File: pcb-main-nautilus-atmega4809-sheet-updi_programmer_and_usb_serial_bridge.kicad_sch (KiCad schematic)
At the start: 7 parts, among them U3 ATSAMD11D14A-SS

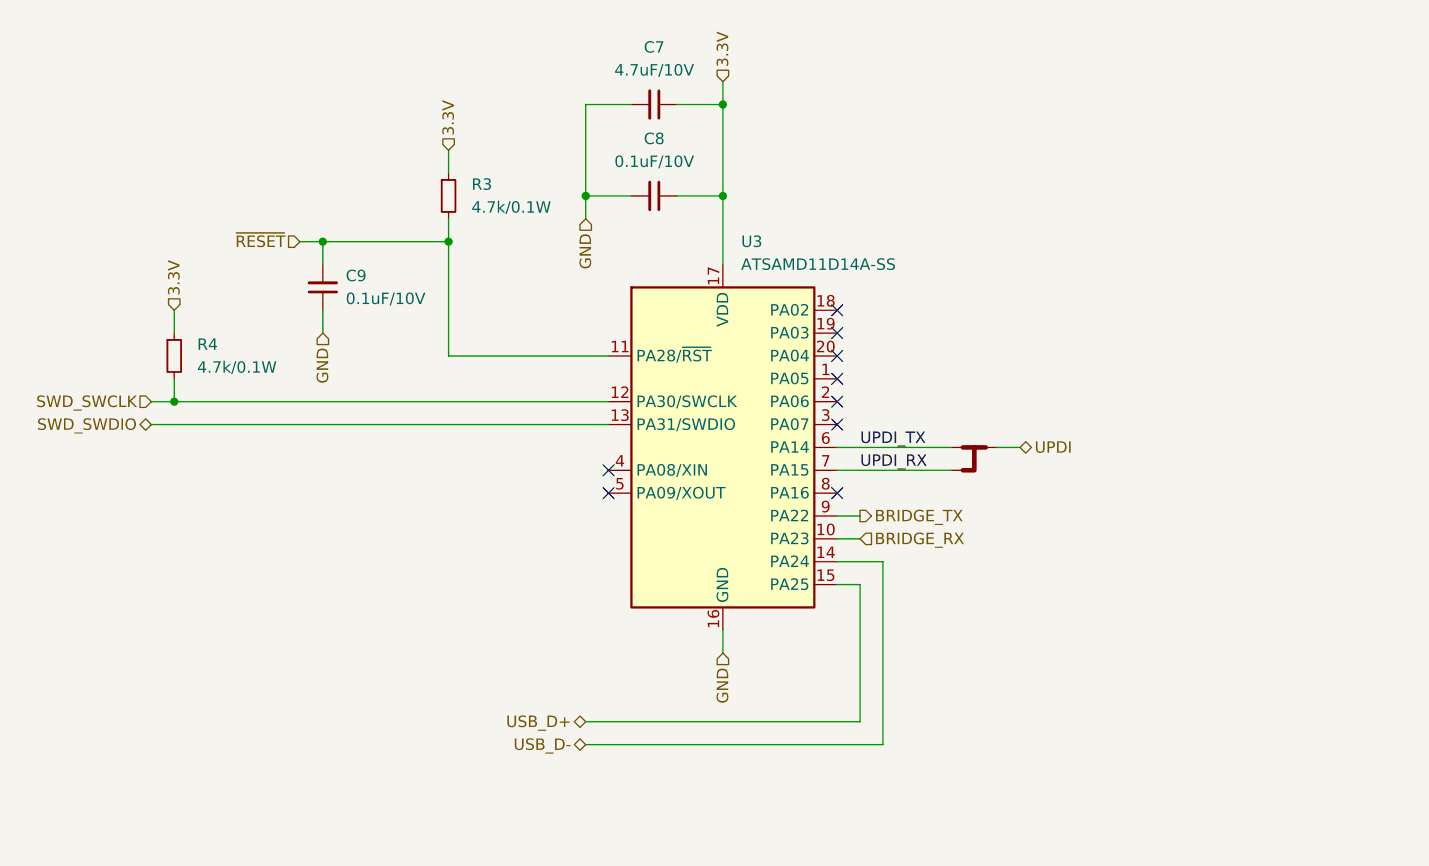
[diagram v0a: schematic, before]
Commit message: Improve UDPI programmer and USB-serial bridge sheet flow
Supports #2.
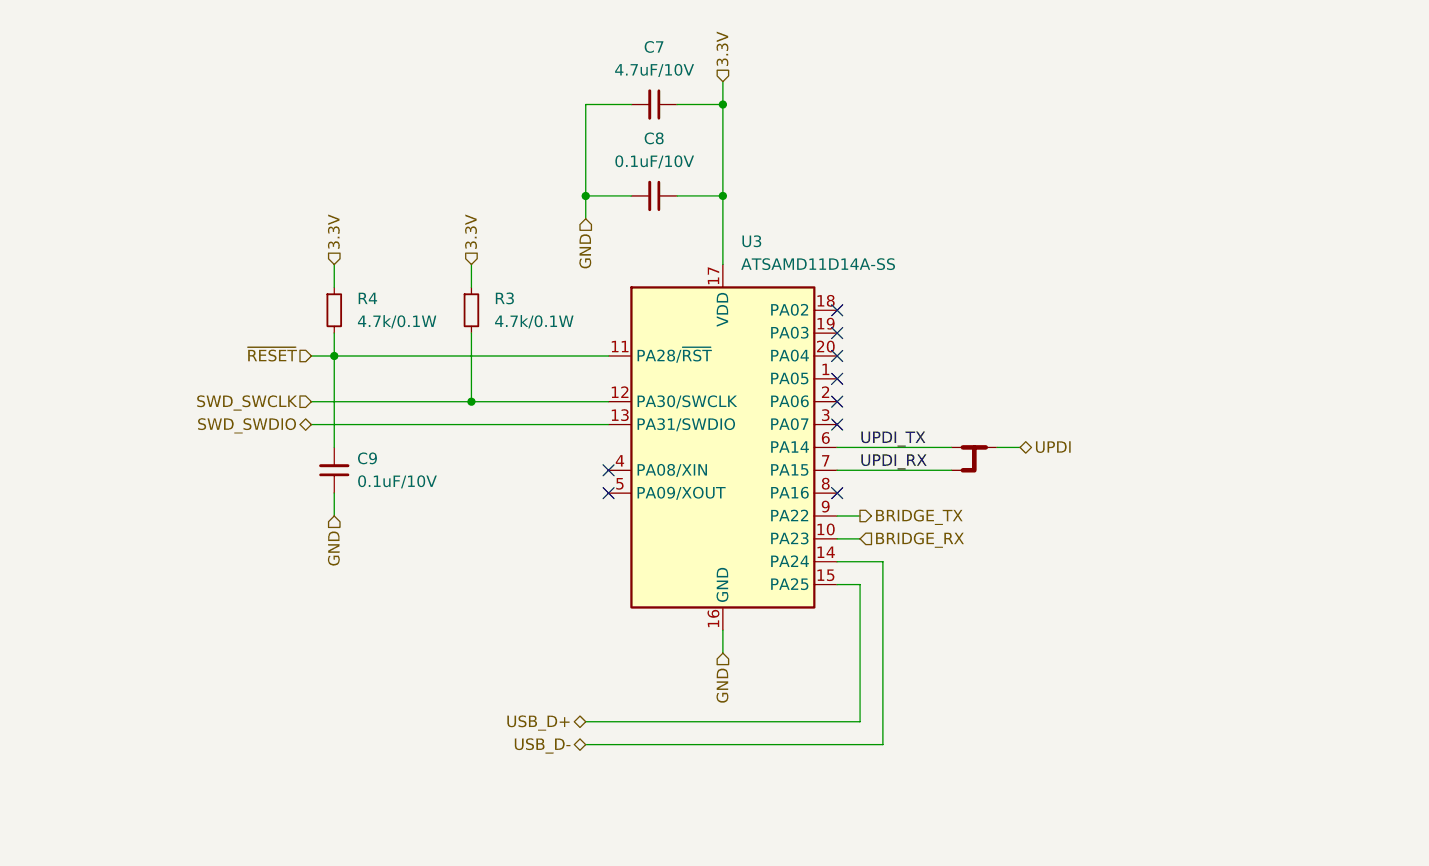
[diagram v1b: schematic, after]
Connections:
- net SWD_SWCLK: now also R3.2; no longer R4.2
- net ~{RESET}: now also R4.2; no longer R3.2
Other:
- moved on the sheet: C9, R3, R4

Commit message: Update schematic annotations
Supports #2.
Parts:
- renumbered R4 to R3, R3 to R4
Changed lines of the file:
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@@
   (symbol (lib_id "Device:R_Small") (at 111.76 86.36 0) (unit 1)
     (in_bom yes) (on_board yes) (fields_autoplaced)
-    (property "Reference" "R3" (id 0) (at 114.3 85.0899 0)
+    (property "Reference" "R4" (id 0) (at 114.3 85.0899 0)
       (effects (font (size 1.27 1.27)) (justify left))
     )
@@
   (symbol (lib_id "Device:R_Small") (at 96.52 86.36 0) (unit 1)
     (in_bom yes) (on_board yes) (fields_autoplaced)
-    (property "Reference" "R4" (id 0) (at 99.06 85.0899 0)
+    (property "Reference" "R3" (id 0) (at 99.06 85.0899 0)
       (effects (font (size 1.27 1.27)) (justify left))
     )

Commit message: Connect root sheet
Supports #2.
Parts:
- renumbered C9 to C10, C7 to C8, C8 to C9, R3 to R4, R4 to R5
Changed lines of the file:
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@@
   (symbol (lib_id "Device:C_Small") (at 96.52 104.14 180) (unit 1)
     (in_bom yes) (on_board yes) (fields_autoplaced)
-    (property "Reference" "C9" (id 0) (at 99.06 102.8635 0)
+    (property "Reference" "C10" (id 0) (at 99.06 102.8635 0)
       (effects (font (size 1.27 1.27)) (justify right))
     )
@@
   (symbol (lib_id "Device:C_Small") (at 132.08 73.66 270) (unit 1)
     (in_bom yes) (on_board yes) (fields_autoplaced)
-    (property "Reference" "C8" (id 0) (at 132.0736 67.31 90))
+    (property "Reference" "C9" (id 0) (at 132.0736 67.31 90))
     (property "Value" "0.1uF/10V" (id 1) (at 132.0736 69.85 90))
     (property "Footprint" "Capacitor_SMD:C_0603_1608Metric_Pad1.08x0.95mm_HandSolder" (id 2) (at 132.08 73.66 0)
@@
   (symbol (lib_id "Device:R_Small") (at 111.76 86.36 0) (unit 1)
     (in_bom yes) (on_board yes) (fields_autoplaced)
-    (property "Reference" "R4" (id 0) (at 114.3 85.0899 0)
+    (property "Reference" "R5" (id 0) (at 114.3 85.0899 0)
       (effects (font (size 1.27 1.27)) (justify left))
     )
@@
   (symbol (lib_id "Device:C_Small") (at 132.08 63.5 270) (unit 1)
     (in_bom yes) (on_board yes) (fields_autoplaced)
-    (property "Reference" "C7" (id 0) (at 132.0736 57.15 90))
+    (property "Reference" "C8" (id 0) (at 132.0736 57.15 90))
     (property "Value" "4.7uF/10V" (id 1) (at 132.0736 59.69 90))
     (property "Footprint" "Capacitor_SMD:C_0603_1608Metric_Pad1.08x0.95mm_HandSolder" (id 2) (at 132.08 63.5 0)
@@
   (symbol (lib_id "Device:R_Small") (at 96.52 86.36 0) (unit 1)
     (in_bom yes) (on_board yes) (fields_autoplaced)
-    (property "Reference" "R3" (id 0) (at 99.06 85.0899 0)
+    (property "Reference" "R4" (id 0) (at 99.06 85.0899 0)
       (effects (font (size 1.27 1.27)) (justify left))
     )

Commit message: Nest level shifter sheets under UPDI programmer and bridge sheet
Supports #2.
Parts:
- renumbered C9 to C10, C10 to C8, C8 to C9
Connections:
- net BRIDGE_RX: no longer U3.10 (PA23)
- net BRIDGE_TX: no longer U3.9 (PA22)
- net UPDI: no longer NT1.2
- new net BI-DIRECTIONAL LEVEL SHIFTER: RX-TX/SIGNAL_3.3V: U3.10 (PA23)
- new net BI-DIRECTIONAL LEVEL SHIFTER: TX-RX/SIGNAL_3.3V: U3.9 (PA22)
- new net BI-DIRECTIONAL LEVEL SHIFTER: UPDI/SIGNAL_3.3V: NT1.2
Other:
- added sheet BI-DIRECTIONAL LEVEL SHIFTER: RX-TX (pcb-main-nautilus-atmega4809-sheet-bi_directional_level_shifter.kicad_sch)
- added sheet BI-DIRECTIONAL LEVEL SHIFTER: TX-RX (pcb-main-nautilus-atmega4809-sheet-bi_directional_level_shifter.kicad_sch)
- added sheet BI-DIRECTIONAL LEVEL SHIFTER: UPDI (pcb-main-nautilus-atmega4809-sheet-bi_directional_level_shifter.kicad_sch)
- moved on the sheet: C10, C8, C9, R4, R5, U3

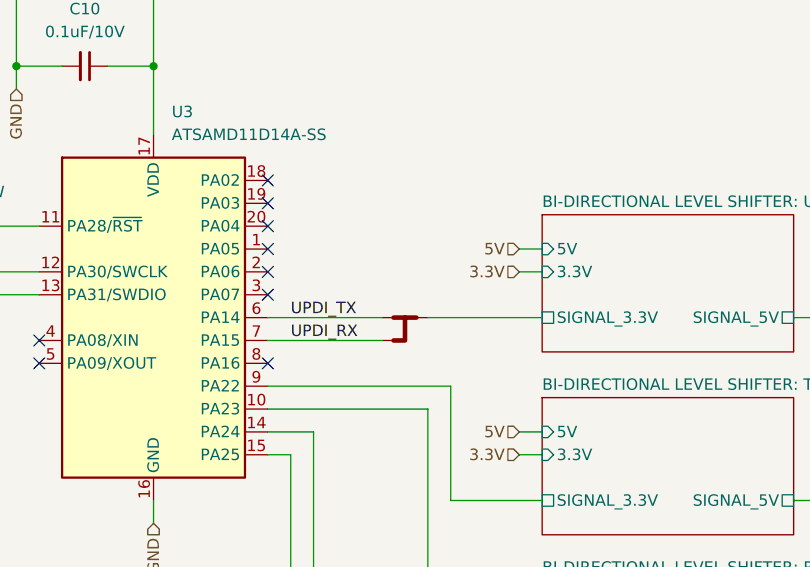
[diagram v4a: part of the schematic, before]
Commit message: Fix NetTie usage
Supports #2.
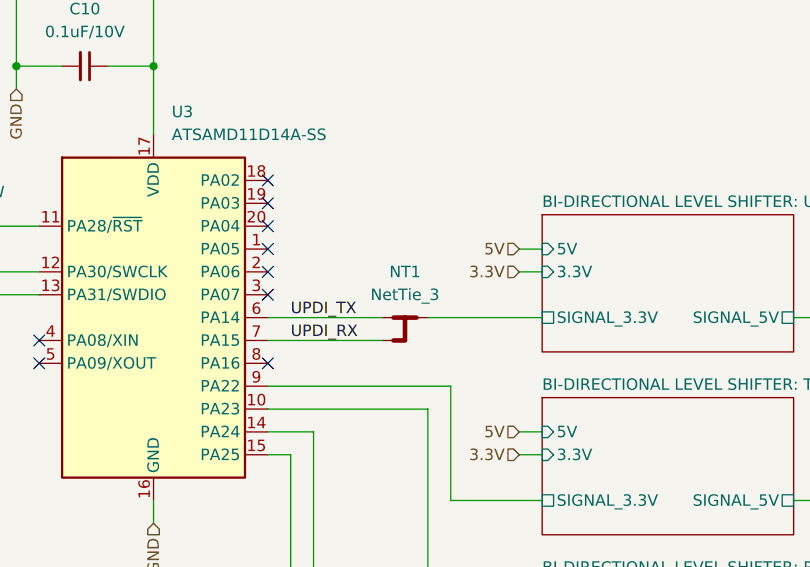
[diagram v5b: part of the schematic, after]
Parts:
- NT1: now in the parts list
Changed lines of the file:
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@@
   )
   (symbol (lib_id "Device:NetTie_3") (at 149.86 101.6 0) (unit 1)
-    (in_bom no) (on_board yes) (fields_autoplaced)
-    (property "Reference" "NT1" (id 0) (at 149.86 96.52 0)
-      (effects (font (size 1.27 1.27)) hide)
-    )
-    (property "Value" "NetTie_3" (id 1) (at 149.86 99.06 0)
-      (effects (font (size 1.27 1.27)) hide)
-    )
+    (in_bom yes) (on_board yes) (fields_autoplaced)
+    (property "Reference" "NT1" (id 0) (at 149.86 96.52 0))
+    (property "Value" "NetTie_3" (id 1) (at 149.86 99.06 0))
     (property "Footprint" "NetTie:NetTie-3_SMD_Pad0.5mm" (id 2) (at 149.86 101.6 0)
       (effects (font (size 1.27 1.27)) hide)

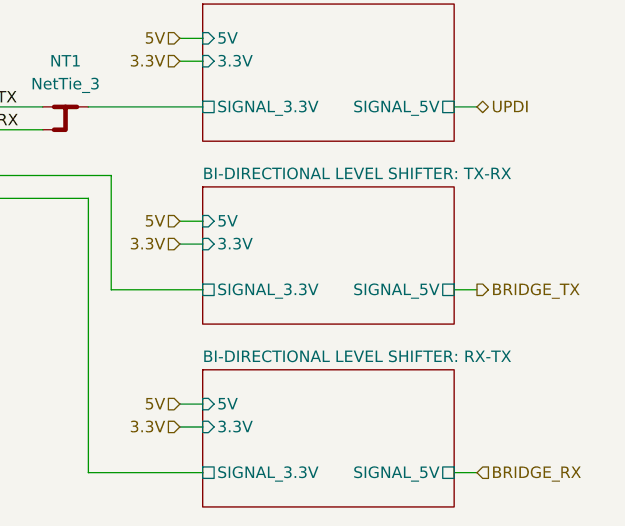
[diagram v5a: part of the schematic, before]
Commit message: Rename serial signals
Supports #2.
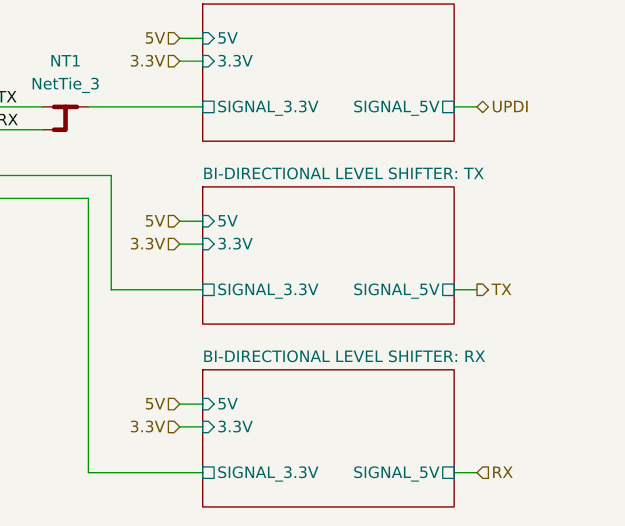
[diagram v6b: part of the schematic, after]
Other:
- sheet BI-DIRECTIONAL LEVEL SHIFTER: RX-TX renamed BI-DIRECTIONAL LEVEL SHIFTER: RX
- sheet BI-DIRECTIONAL LEVEL SHIFTER: TX-RX renamed BI-DIRECTIONAL LEVEL SHIFTER: TX
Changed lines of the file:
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@@
     (effects (font (size 1.27 1.27)) (justify right))
   )
-  (hierarchical_label "BRIDGE_TX" (shape output) (at 195.58 121.92 0)
+  (hierarchical_label "TX" (shape output) (at 195.58 121.92 0)
     (effects (font (size 1.27 1.27)) (justify left))
   )
@@
     (effects (font (size 1.27 1.27)) (justify right))
   )
-  (hierarchical_label "BRIDGE_RX" (shape input) (at 195.58 142.24 0)
+  (hierarchical_label "RX" (shape input) (at 195.58 142.24 0)
     (effects (font (size 1.27 1.27)) (justify left))
   )
@@
     (stroke (width 0.1524) (type solid) (color 0 0 0 0))
     (fill (color 0 0 0 0.0000))
-    (property "Sheet name" "BI-DIRECTIONAL LEVEL SHIFTER: TX-RX" (id 0) (at 165.1 109.7784 0)
+    (property "Sheet name" "BI-DIRECTIONAL LEVEL SHIFTER: TX" (id 0) (at 165.1 109.7784 0)
       (effects (font (size 1.27 1.27)) (justify left bottom))
     )
@@
     (stroke (width 0.1524) (type solid) (color 0 0 0 0))
     (fill (color 0 0 0 0.0000))
-    (property "Sheet name" "BI-DIRECTIONAL LEVEL SHIFTER: RX-TX" (id 0) (at 165.1 130.0984 0)
+    (property "Sheet name" "BI-DIRECTIONAL LEVEL SHIFTER: RX" (id 0) (at 165.1 130.0984 0)
       (effects (font (size 1.27 1.27)) (justify left bottom))
     )

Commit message: Update BOM
Supports #2.
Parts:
- C9: Mouser Part Number 80-C0603C106M9PAC -> 80-C0603C475M8PACLR
- R4, R5: Manufacturer Part Number ERJ-3EKF4701V -> ERJ-3EKF4701
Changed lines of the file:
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@@
       (effects (font (size 1.27 1.27)) hide)
     )
-    (property "Manufacturer Part Number" "ERJ-3EKF4701V" (id 5) (at 93.98 86.36 0)
+    (property "Manufacturer Part Number" "ERJ-3EKF4701" (id 5) (at 93.98 86.36 0)
       (effects (font (size 1.27 1.27)) hide)
     )
@@
       (effects (font (size 1.27 1.27)) hide)
     )
-    (property "Datasheet" "https://connect.kemet.com:7667/gateway/IntelliData-ComponentDocumentation/1.0/download/datasheet/C0603C104M8RACTU" (id 3) (at 114.3 63.5 0)
+    (property "Datasheet" "https://connect.kemet.com:7667/gateway/IntelliData-ComponentDocumentation/1.0/download/datasheet/C0603C475M8PACTU" (id 3) (at 114.3 63.5 0)
       (effects (font (size 1.27 1.27)) hide)
     )
@@
       (effects (font (size 1.27 1.27)) hide)
     )
-    (property "Mouser Part Number" "80-C0603C106M9PAC" (id 7) (at 114.3 63.5 0)
+    (property "Mouser Part Number" "80-C0603C475M8PACLR" (id 7) (at 114.3 63.5 0)
       (effects (font (size 1.27 1.27)) hide)
     )
@@
       (effects (font (size 1.27 1.27)) hide)
     )
-    (property "Manufacturer Part Number" "ERJ-3EKF4701V" (id 5) (at 78.74 86.36 0)
+    (property "Manufacturer Part Number" "ERJ-3EKF4701" (id 5) (at 78.74 86.36 0)
       (effects (font (size 1.27 1.27)) hide)
     )

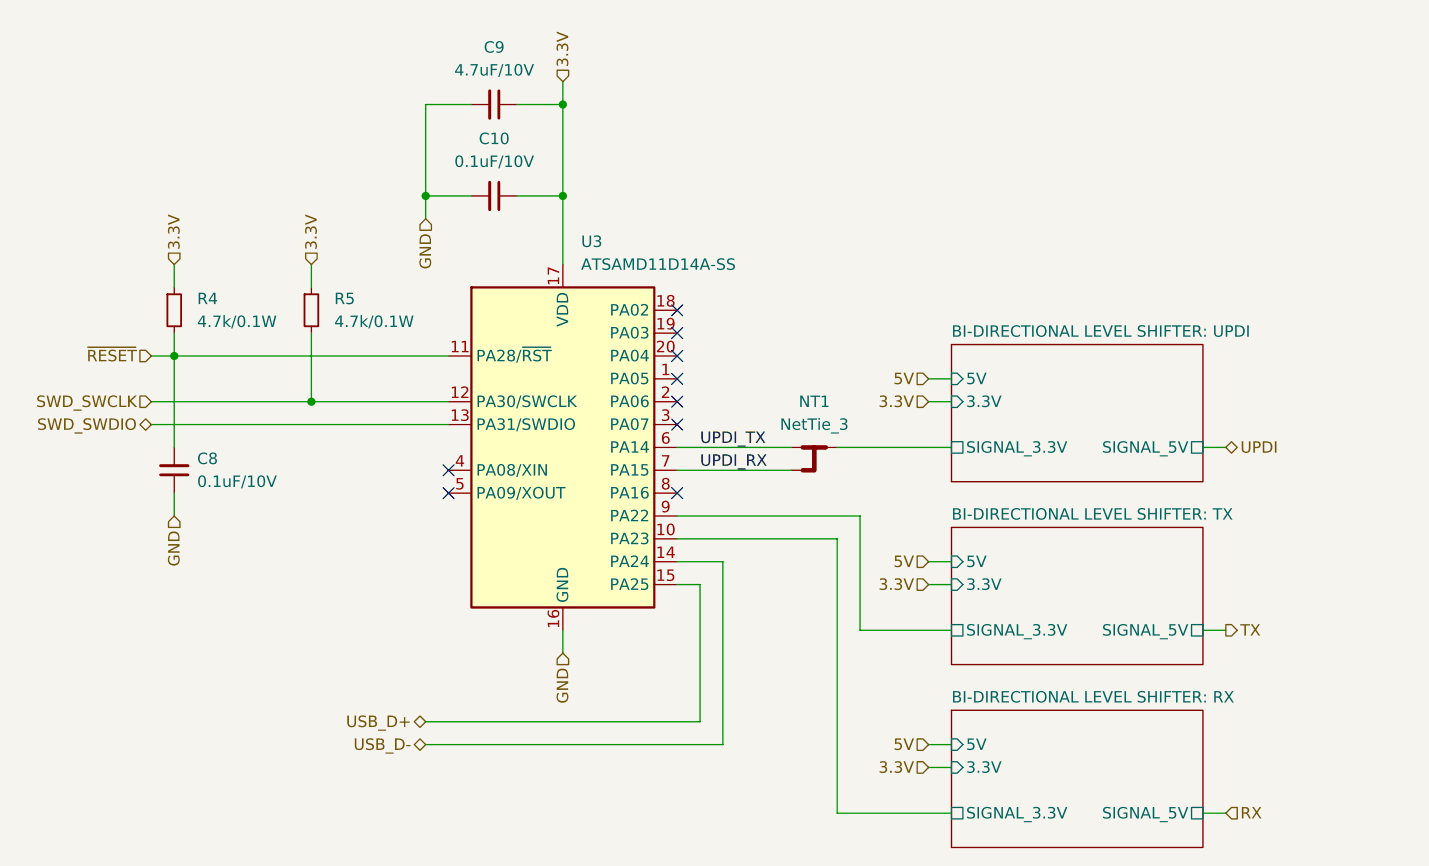
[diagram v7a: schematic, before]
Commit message: Remove improperly used netties
Supports #2.
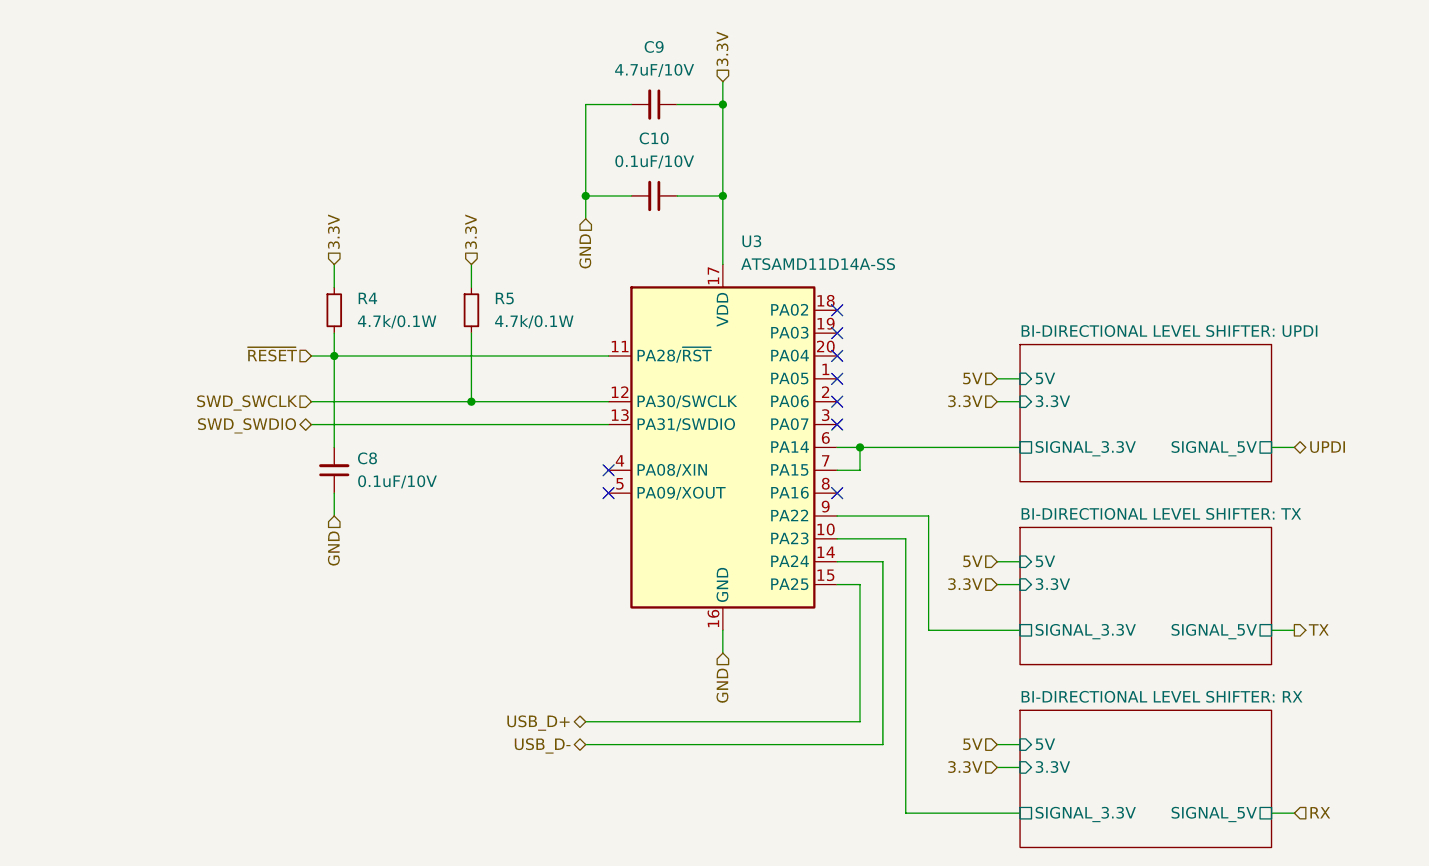
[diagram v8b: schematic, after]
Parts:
- removed NT1: NetTie_3, NetTie:NetTie-3_SMD_Pad0.5mm, symbol Device:NetTie_3
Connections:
- net UPDI_RX is gone; now on net BI-DIRECTIONAL LEVEL SHIFTER: UPDI/SIGNAL_3.3V: U3.7 (PA15)
- net UPDI_TX is gone; now on net BI-DIRECTIONAL LEVEL SHIFTER: UPDI/SIGNAL_3.3V: U3.6 (PA14)
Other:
- moved on the sheet: C10, C8, C9, R4, R5, U3
